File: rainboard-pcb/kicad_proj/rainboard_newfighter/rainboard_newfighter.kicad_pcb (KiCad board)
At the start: 2 copper layers, 260 x 253.6 mm, 97 parts, among them J1 Conn_01x02, J10 Conn_01x03, J11 SDS-50J, J12 SDS-50J, J13 Conn_01x02, J14 Conn_01x02, J15 Conn_01x02, J16 Conn_01x02, J2 Conn_01x02, J3 Conn_01x02, J4 Conn_01x02, J5 Conn_01x02, J6 Conn_01x02, J7 Conn_01x02, J8 Conn_01x02, U1 MCP23017-E_SO, U2 74HC14D, U3 6N138SDM

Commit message: Schematic nearly finalized; PCB / footprint started
-Schematic is nearly finished. Needs some footprint associations and verifications.
-A few open questions remain.
-some lib updates to go w/ sch improvements
-
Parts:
- added C1: 10uF 25V, Capacitor_SMD:C_1206_3216Metric, F.Cu at (150.9, -87.0)
- added C10: 1uF 25V, Capacitor_SMD:C_0805_2012Metric, F.Cu at (167.7, -96.4)
- added C100: 10uF 25V, Capacitor_SMD:C_1206_3216Metric, F.Cu at (135.9, -76.4)
- added C101: 10uF 25V, Capacitor_SMD:C_1206_3216Metric, F.Cu at (135.9, -79.7)
- added C102: 100nf, Capacitor_SMD:C_0603_1608Metric, F.Cu at (290.8, -123.2)
- added C103: 100nf, Capacitor_SMD:C_0603_1608Metric, F.Cu at (204.9, -40.8)
- added C104: 100nf, Capacitor_SMD:C_0603_1608Metric, F.Cu at (264.7, -99.9)
- added C105: 100nf, Capacitor_SMD:C_0603_1608Metric, F.Cu at (232.7, -69.2)
- added C106: 100nf, Capacitor_SMD:C_0603_1608Metric, F.Cu at (250.9, -83.4)
- added C107: 100nf, Capacitor_SMD:C_0603_1608Metric, F.Cu at (220.9, -51.6)
- added C108: 100nf, Capacitor_SMD:C_0603_1608Metric, F.Cu at (280.7, -110.7)
- added C109: 100nf, Capacitor_SMD:C_0603_1608Metric, F.Cu at (201.1, -30.5)
- added C11: 1uF 25V, Capacitor_SMD:C_0805_2012Metric, F.Cu at (172.4, 57.7)
- added C110: 100nf, Capacitor_SMD:C_0603_1608Metric, F.Cu at (250.9, -73.1)
- added C111: 100nf, Capacitor_SMD:C_0603_1608Metric, F.Cu at (306.9, -123.2)
- added C112: 100nf, Capacitor_SMD:C_0603_1608Metric, F.Cu at (185.1, -36.5)
- added C113: 100nf, Capacitor_SMD:C_0603_1608Metric, F.Cu at (280.7, -100.4)
- added C114: 100nf, Capacitor_SMD:C_0603_1608Metric, F.Cu at (217.1, -20.2)
- added C115: 100nf, Capacitor_SMD:C_0603_1608Metric, F.Cu at (266.9, -69.0)
- added C116: 100nf, Capacitor_SMD:C_0603_1608Metric, F.Cu at (237.0, -38.2)
- added C117: 100nf, Capacitor_SMD:C_0603_1608Metric, F.Cu at (322.9, -123.2)
- added C118: 100nf, Capacitor_SMD:C_0603_1608Metric, F.Cu at (283.0, -90.1)
- added C119: 100nf, Capacitor_SMD:C_0603_1608Metric, F.Cu at (237.0, -48.5)
- added C12: 100nf, Capacitor_SMD:C_0603_1608Metric, F.Cu at (186.7, -101.8)
- added C120: 100nf, Capacitor_SMD:C_0603_1608Metric, F.Cu at (266.9, -79.3)
- added C121: 100nf, Capacitor_SMD:C_0603_1608Metric, F.Cu at (217.1, -30.5)
- added C122: 100nf, Capacitor_SMD:C_0603_1608Metric, F.Cu at (296.8, -112.9)
- added C123: 100nf, Capacitor_SMD:C_0603_1608Metric, F.Cu at (237.0, -58.8)
- added C124: 100nf, Capacitor_SMD:C_0603_1608Metric, F.Cu at (266.9, -89.6)
- added C125: 100nf, Capacitor_SMD:C_0603_1608Metric, F.Cu at (220.9, -41.3)
- added C126: 100nf, Capacitor_SMD:C_0603_1608Metric, F.Cu at (269.0, -48.3)
- added C127: 100nf, Capacitor_SMD:C_0603_1608Metric, F.Cu at (312.8, -112.9)
- added C128: 100nf, Capacitor_SMD:C_0603_1608Metric, F.Cu at (283.0, -79.8)
- added C129: 100nf, Capacitor_SMD:C_0603_1608Metric, F.Cu at (253.0, -58.6)
- added C13: 1uF 25V, Capacitor_SMD:C_0805_2012Metric, F.Cu at (176.8, 57.7)
- added C130: 100nf, Capacitor_SMD:C_0603_1608Metric, F.Cu at (299.0, -92.3)
- added C131: 100nf, Capacitor_SMD:C_0603_1608Metric, F.Cu at (253.0, -48.3)
- added C132: 100nf, Capacitor_SMD:C_0603_1608Metric, F.Cu at (233.1, -27.9)
- added C133: 100nf, Capacitor_SMD:C_0603_1608Metric, F.Cu at (253.0, -38.0)
- added C134: 100nf, Capacitor_SMD:C_0603_1608Metric, F.Cu at (269.0, -58.6)
- added C135: 100nf, Capacitor_SMD:C_0603_1608Metric, F.Cu at (283.0, -69.5)
- added C136: 100nf, Capacitor_SMD:C_0603_1608Metric, F.Cu at (312.8, -102.6)
- added C137: 100nf, Capacitor_SMD:C_0603_1608Metric, F.Cu at (328.8, -112.9)
- added C138: 100nf, Capacitor_SMD:C_0603_1608Metric, F.Cu at (299.0, -82.0)
- added C139: 100nf, Capacitor_SMD:C_0603_1608Metric, F.Cu at (315.0, -92.3)
- added C14: 470uF 25V, Capacitor_SMD:CP_Elec_10x10, F.Cu at (236.1, -5.10)
- added C140: 100nf, Capacitor_SMD:C_0603_1608Metric, F.Cu at (296.8, -102.6)
- added C141: 100nf, Capacitor_SMD:C_0603_1608Metric, F.Cu at (249.1, -27.7)
- added C142: 100nf, Capacitor_SMD:C_0603_1608Metric, F.Cu at (269.0, -38.0)
- added C143: 100nf, Capacitor_SMD:C_0603_1608Metric, F.Cu at (299.0, -71.6)
- added C144: 100nf, Capacitor_SMD:C_0603_1608Metric, F.Cu at (328.8, -102.6)
- added C145: 100nf, Capacitor_SMD:C_0603_1608Metric, F.Cu at (285.0, -59.1)
- added C146: 100nf, Capacitor_SMD:C_0603_1608Metric, F.Cu at (315.0, -82.0)
- added C147: 100nf, Capacitor_SMD:C_0603_1608Metric, F.Cu at (331.0, -92.3)
- added C148: 100nf, Capacitor_SMD:C_0603_1608Metric, F.Cu at (285.0, -48.8)
- added C149: 100nf, Capacitor_SMD:C_0603_1608Metric, F.Cu at (265.2, -27.7)
- added C15: 1uF 25V, Capacitor_SMD:C_0805_2012Metric, F.Cu at (188.0, -118.1)
- added C150: 100nf, Capacitor_SMD:C_0603_1608Metric, F.Cu at (285.0, -38.5)
- added C151: 100nf, Capacitor_SMD:C_0603_1608Metric, F.Cu at (315.0, -71.6)
- added C152: 100nf, Capacitor_SMD:C_0603_1608Metric, F.Cu at (301.0, -61.3)
- added C153: 100nf, Capacitor_SMD:C_0603_1608Metric, F.Cu at (331.0, -82.0)
- added C154: 100nf, Capacitor_SMD:C_0603_1608Metric, F.Cu at (201.1, -20.2)
- added C155: 100nf, Capacitor_SMD:C_0603_1608Metric, F.Cu at (244.0, -93.7)
- added C156: 100nf, Capacitor_SMD:C_0603_1608Metric, F.Cu at (264.7, -110.2)
- added C157: 100nf, Capacitor_SMD:C_0603_1608Metric, F.Cu at (204.9, -51.1)
- added C158: 100nf, Capacitor_SMD:C_0603_1608Metric, F.Cu at (185.1, -26.2)
- added C16: 22PF, Capacitor_SMD:C_0603_1608Metric, F.Cu at (184.2, -99.1)
- added C17: 22PF, Capacitor_SMD:C_0603_1608Metric, F.Cu at (193.1, -107.9)
- added C18: 1uF 25V, Capacitor_SMD:C_0805_2012Metric, F.Cu at (179.5, -110.8)
- added C19: 100nf, Capacitor_SMD:C_0603_1608Metric, F.Cu at (188.7, -104.3)
- added C20: 470uF 25V, Capacitor_SMD:CP_Elec_10x10, F.Cu at (236.1, 6.75)
- added C21: 1uF 25V, Capacitor_SMD:C_0805_2012Metric, F.Cu at (155.9, -85.9)
- added C22: 10uF 25V, Capacitor_SMD:C_1206_3216Metric, F.Cu at (180.1, -114.0)
- added C23: 1uF 25V, Capacitor_SMD:C_0805_2012Metric, F.Cu at (181.2, 57.7)
- added C24: 10uF 25V, Capacitor_SMD:C_1206_3216Metric, F.Cu at (156.9, -92.9)
- added C25: 10uF 25V, Capacitor_SMD:C_1206_3216Metric, F.Cu at (150.9, -90.3)
- added C26: 10uF 25V, Capacitor_SMD:C_1206_3216Metric, F.Cu at (160.0, -111.3)
- added C27: 10uF 25V, Capacitor_SMD:C_1206_3216Metric, F.Cu at (162.7, -96.3)
- added C28: 1uF 25V, Capacitor_SMD:C_0805_2012Metric, F.Cu at (194.5, -121.4)
- added C29: 100nf, Capacitor_SMD:C_0603_1608Metric, F.Cu at (182.7, -101.6)
- added C3: 10uF 25V, Capacitor_SMD:C_1206_3216Metric, F.Cu at (182.9, -117.6)
- added C30: 10uF 25V, Capacitor_SMD:C_1206_3216Metric, F.Cu at (190.7, -125.8)
- added C31: 100nf, Capacitor_SMD:C_0603_1608Metric, F.Cu at (197.7, -116.2)
- added C32: 470uF 25V, Capacitor_SMD:CP_Elec_10x10, F.Cu at (250.2, -5.10)
- added C33: 100nf, Capacitor_SMD:C_0603_1608Metric, F.Cu at (188.7, -106.8)
- added C34: 22PF, Capacitor_SMD:C_0603_1608Metric, F.Cu at (180.2, -99.1)
- added C35: 22PF, Capacitor_SMD:C_0603_1608Metric, F.Cu at (189.1, -109.3)
- added C36: 1uF 25V, Capacitor_SMD:C_0805_2012Metric, F.Cu at (192.4, -118.1)
- added C37: 100nf, Capacitor_SMD:C_0603_1608Metric, F.Cu at (203.9, -123.2)
- added C38: 470uF 25V, Capacitor_SMD:CP_Elec_10x10, F.Cu at (250.2, 6.75)
- added C39: 100nf, Capacitor_SMD:C_0603_1608Metric, F.Cu at (160.1, -85.9)
- added C40: 100nf, Capacitor_SMD:C_0603_1608Metric, F.Cu at (176.2, -97.2)
- added C41: 100nf, Capacitor_SMD:C_0603_1608Metric, F.Cu at (193.7, -115.4)
- added C42: 1uF 25V, Capacitor_SMD:C_0805_2012Metric, F.Cu at (180.5, -107.9)
- added C43: 100nf, Capacitor_SMD:C_0603_1608Metric, F.Cu at (170.7, -93.0)
- added C44: 100nf, Capacitor_SMD:C_0603_1608Metric, F.Cu at (178.7, -101.6)
- added C45: 10uF 25V, Capacitor_SMD:C_1206_3216Metric, F.Cu at (226.8, -119.2)
- added C46: 10uF 25V, Capacitor_SMD:C_1206_3216Metric, F.Cu at (215.6, -125.8)
- added C47: 10uF 25V, Capacitor_SMD:C_1206_3216Metric, F.Cu at (221.2, -115.9)
- added C48: 10uF 25V, Capacitor_SMD:C_1206_3216Metric, F.Cu at (232.4, -125.8)
- added C49: 10uF 25V, Capacitor_SMD:C_1206_3216Metric, F.Cu at (226.8, -122.5)
- added C5: 1uF 25V, Capacitor_SMD:C_0805_2012Metric, F.Cu at (189.2, 54.5)
- added C50: 10uF 25V, Capacitor_SMD:C_1206_3216Metric, F.Cu at (221.2, -119.2)
- added C51: 10uF 25V, Capacitor_SMD:C_1206_3216Metric, F.Cu at (215.6, -115.9)
- added C52: 10uF 25V, Capacitor_SMD:C_1206_3216Metric, F.Cu at (226.8, -125.8)
- added C53: 10uF 25V, Capacitor_SMD:C_1206_3216Metric, F.Cu at (221.2, -122.5)
- added C54: 10uF 25V, Capacitor_SMD:C_1206_3216Metric, F.Cu at (215.6, -119.2)
- added C55: 10uF 25V, Capacitor_SMD:C_1206_3216Metric, F.Cu at (221.2, -125.8)
- added C56: 10uF 25V, Capacitor_SMD:C_1206_3216Metric, F.Cu at (215.6, -122.5)
- added C57: DNP-10uF 25V, Capacitor_SMD:C_1206_3216Metric, F.Cu at (215.6, -89.7)
- added C58: 1uF 25V, Capacitor_SMD:C_0805_2012Metric, F.Cu at (220.6, -89.8)
- added C59: DNP-10uF 25V, Capacitor_SMD:C_1206_3216Metric, F.Cu at (236.3, -102.7)
- added C6: 10uF 25V, Capacitor_SMD:C_1206_3216Metric, F.Cu at (182.9, -120.8)
- added C60: 1uF 25V, Capacitor_SMD:C_0805_2012Metric, F.Cu at (244.2, -109.5)
- added C61: DNP-10uF 25V, Capacitor_SMD:C_1206_3216Metric, F.Cu at (135.9, -44.9)
- added C62: 1uF 25V, Capacitor_SMD:C_0805_2012Metric, F.Cu at (140.9, -45.1)
- added C63: DNP-10uF 25V, Capacitor_SMD:C_1206_3216Metric, F.Cu at (183.5, -73.1)
- added C64: 1uF 25V, Capacitor_SMD:C_0805_2012Metric, F.Cu at (188.5, -73.2)
- added C65: DNP-10uF 25V, Capacitor_SMD:C_1206_3216Metric, F.Cu at (135.9, -31.9)
- added C66: 1uF 25V, Capacitor_SMD:C_0805_2012Metric, F.Cu at (143.7, -38.7)
- added C67: DNP-10uF 25V, Capacitor_SMD:C_1206_3216Metric, F.Cu at (215.6, -102.7)
- added C68: 1uF 25V, Capacitor_SMD:C_0805_2012Metric, F.Cu at (223.4, -109.5)
- added C69: DNP-10uF 25V, Capacitor_SMD:C_1206_3216Metric, F.Cu at (156.7, -44.9)
- added C7: 100nf, Capacitor_SMD:C_0603_1608Metric, F.Cu at (180.2, -94.1)
- added C70: 1uF 25V, Capacitor_SMD:C_0805_2012Metric, F.Cu at (164.5, -51.7)
- added C71: DNP-10uF 25V, Capacitor_SMD:C_1206_3216Metric, F.Cu at (242.6, -119.2)
- added C72: 1uF 25V, Capacitor_SMD:C_0805_2012Metric, F.Cu at (250.4, -126.0)
- added C73: DNP-10uF 25V, Capacitor_SMD:C_1206_3216Metric, F.Cu at (135.9, -18.9)
- added C74: 1uF 25V, Capacitor_SMD:C_0805_2012Metric, F.Cu at (143.7, -25.7)
- added C75: DNP-10uF 25V, Capacitor_SMD:C_1206_3216Metric, F.Cu at (183.5, -60.1)
- added C76: 1uF 25V, Capacitor_SMD:C_0805_2012Metric, F.Cu at (191.4, -66.8)
- added C77: DNP-10uF 25V, Capacitor_SMD:C_1206_3216Metric, F.Cu at (204.3, -73.1)
- added C78: 1uF 25V, Capacitor_SMD:C_0805_2012Metric, F.Cu at (212.1, -79.8)
- added C79: DNP-10uF 25V, Capacitor_SMD:C_1206_3216Metric, F.Cu at (156.7, -31.9)
- added C8: 1uF 25V, Capacitor_SMD:C_0805_2012Metric, F.Cu at (166.5, -93.2)
- added C80: 1uF 25V, Capacitor_SMD:C_0805_2012Metric, F.Cu at (161.7, -32.1)
- added C81: 470uF 25V, Capacitor_SMD:CP_Elec_10x10, F.Cu at (236.1, 23.7)
- added C82: 10uF 25V, Capacitor_SMD:C_1206_3216Metric, F.Cu at (225.1, -80.0)
- added C83: 10uF 25V, Capacitor_SMD:C_1206_3216Metric, F.Cu at (225.1, -83.3)
- added C84: 100nf, Capacitor_SMD:C_0603_1608Metric, F.Cu at (203.5, -60.4)
- added C85: 100nf, Capacitor_SMD:C_0603_1608Metric, F.Cu at (155.9, -19.3)
- added C86: 100nf, Capacitor_SMD:C_0603_1608Metric, F.Cu at (275.4, -126.2)
- added C87: 100nf, Capacitor_SMD:C_0603_1608Metric, F.Cu at (189.5, -52.0)
- added C88: 470uF 25V, Capacitor_SMD:CP_Elec_10x10, F.Cu at (285.0, -5.10)
- added C89: 470uF 25V, Capacitor_SMD:CP_Elec_10x10, F.Cu at (285.0, 6.75)
- added C9: 100nf, Capacitor_SMD:C_0603_1608Metric, F.Cu at (201.7, -115.7)
- added C90: 470uF 25V, Capacitor_SMD:CP_Elec_10x10, F.Cu at (299.0, -5.10)
- added C91: 470uF 25V, Capacitor_SMD:CP_Elec_10x10, F.Cu at (299.0, 6.75)
- added C92: 10uF 25V, Capacitor_SMD:C_1206_3216Metric, F.Cu at (135.9, -66.5)
- added C93: 10uF 25V, Capacitor_SMD:C_1206_3216Metric, F.Cu at (147.1, -76.4)
- added C94: 10uF 25V, Capacitor_SMD:C_1206_3216Metric, F.Cu at (141.5, -73.1)
- added C95: 10uF 25V, Capacitor_SMD:C_1206_3216Metric, F.Cu at (135.9, -69.8)
- added C96: 10uF 25V, Capacitor_SMD:C_1206_3216Metric, F.Cu at (147.1, -79.7)
- added C97: 10uF 25V, Capacitor_SMD:C_1206_3216Metric, F.Cu at (141.5, -76.4)
- added C98: 10uF 25V, Capacitor_SMD:C_1206_3216Metric, F.Cu at (135.9, -73.1)
- added C99: 10uF 25V, Capacitor_SMD:C_1206_3216Metric, F.Cu at (141.5, -79.7)
- added D1: 12Vw, Diode_SMD:D_SMA, F.Cu at (137.1, -87.5)
- added D10: 40V 1A, Diode_SMD:D_SOD-123, F.Cu at (157.0, -96.3)
- added D11: 40V 1A, Diode_SMD:D_SOD-123, F.Cu at (153.0, -99.6)
- added D12: 40V 1A, Diode_SMD:D_SOD-123, F.Cu at (174.3, -110.6)
- added D13: 5Vw, Package_TO_SOT_SMD:SOT-23, F.Cu at (176.1, -106.6)
- added D14: 40V 1A, Diode_SMD:D_SOD-123, F.Cu at (154.3, -111.3)
- added D15: 5Vw, Package_TO_SOT_SMD:SOT-23, F.Cu at (162.1, -92.4)
- added D16: 5Vw, Package_TO_SOT_SMD:SOT-23, F.Cu at (190.1, -121.9)
- added D17: 40V 1A, Diode_SMD:D_SOD-123, F.Cu at (158.8, -99.6)
- added D18: 40V 1A, Diode_SMD:D_SOD-123, F.Cu at (165.0, -100.7)
- added D19: WS2812B, LED_SMD:LED_WS2812B_PLCC4_5.0x5.0mm_P3.2mm, F.Cu at (217.0, -94.6)
- added D2: 5Vw, Package_TO_SOT_SMD:SOT-23, F.Cu at (185.1, -113.6)
- added D20: WS2812B, LED_SMD:LED_WS2812B_PLCC4_5.0x5.0mm_P3.2mm, F.Cu at (237.7, -107.6)
- added D21: WS2812B, LED_SMD:LED_WS2812B_PLCC4_5.0x5.0mm_P3.2mm, F.Cu at (0.47, -93.5)
- added D22: WS2812B, LED_SMD:LED_WS2812B_PLCC4_5.0x5.0mm_P3.2mm, F.Cu at (184.9, -78.0)
- added D23: WS2812B, LED_SMD:LED_WS2812B_PLCC4_5.0x5.0mm_P3.2mm, F.Cu at (137.3, -36.9)
- added D24: WS2812B, LED_SMD:LED_WS2812B_PLCC4_5.0x5.0mm_P3.2mm, F.Cu at (217.0, -107.6)
- added D25: WS2812B, LED_SMD:LED_WS2812B_PLCC4_5.0x5.0mm_P3.2mm, F.Cu at (158.1, -49.9)
- added D26: WS2812B, LED_SMD:LED_WS2812B_PLCC4_5.0x5.0mm_P3.2mm, F.Cu at (244.0, -124.1)
- added D27: WS2812B, LED_SMD:LED_WS2812B_PLCC4_5.0x5.0mm_P3.2mm, F.Cu at (137.3, -23.9)
- added D28: WS2812B, LED_SMD:LED_WS2812B_PLCC4_5.0x5.0mm_P3.2mm, F.Cu at (184.9, -65.0)
- added D29: WS2812B, LED_SMD:LED_WS2812B_PLCC4_5.0x5.0mm_P3.2mm, F.Cu at (205.7, -78.0)
- added D3: 5Vw, Package_TO_SOT_SMD:SOT-23, F.Cu at (195.7, -125.2)
- added D30: WS2812B, LED_SMD:LED_WS2812B_PLCC4_5.0x5.0mm_P3.2mm, F.Cu at (158.1, -36.9)
- added D31: WS2812B, LED_SMD:LED_WS2812B_PLCC4_5.0x5.0mm_P3.2mm, F.Cu at (205.7, -65.0)
- added D32: WS2812B, LED_SMD:LED_WS2812B_PLCC4_5.0x5.0mm_P3.2mm, F.Cu at (158.1, -23.9)
- added D33: WS2812B, LED_SMD:LED_WS2812B_PLCC4_5.0x5.0mm_P3.2mm, F.Cu at (264.8, -124.1)
- added D34: WS2812B, LED_SMD:LED_WS2812B_PLCC4_5.0x5.0mm_P3.2mm, F.Cu at (178.9, -49.9)
- added D35: WS2812B, LED_SMD:LED_WS2812B_PLCC4_5.0x5.0mm_P3.2mm, F.Cu at (284.6, -124.1)
- added D36: WS2812B, LED_SMD:LED_WS2812B_PLCC4_5.0x5.0mm_P3.2mm, F.Cu at (198.7, -41.7)
- added D37: WS2812B, LED_SMD:LED_WS2812B_PLCC4_5.0x5.0mm_P3.2mm, F.Cu at (258.5, -100.8)
- added D38: WS2812B, LED_SMD:LED_WS2812B_PLCC4_5.0x5.0mm_P3.2mm, F.Cu at (226.5, -70.1)
- added D39: WS2812B, LED_SMD:LED_WS2812B_PLCC4_5.0x5.0mm_P3.2mm, F.Cu at (244.7, -84.3)
- added D4: 5Vw, Diode_SMD:D_SMA, F.Cu at (150.1, -94.2)
- added D40: WS2812B, LED_SMD:LED_WS2812B_PLCC4_5.0x5.0mm_P3.2mm, F.Cu at (214.7, -52.5)
- added D41: WS2812B, LED_SMD:LED_WS2812B_PLCC4_5.0x5.0mm_P3.2mm, F.Cu at (274.5, -111.6)
- added D42: WS2812B, LED_SMD:LED_WS2812B_PLCC4_5.0x5.0mm_P3.2mm, F.Cu at (194.9, -31.4)
- added D43: WS2812B, LED_SMD:LED_WS2812B_PLCC4_5.0x5.0mm_P3.2mm, F.Cu at (244.7, -74.0)
- added D44: WS2812B, LED_SMD:LED_WS2812B_PLCC4_5.0x5.0mm_P3.2mm, F.Cu at (300.6, -124.1)
- added D45: WS2812B, LED_SMD:LED_WS2812B_PLCC4_5.0x5.0mm_P3.2mm, F.Cu at (178.9, -37.4)
- added D46: WS2812B, LED_SMD:LED_WS2812B_PLCC4_5.0x5.0mm_P3.2mm, F.Cu at (274.5, -101.3)
- added D47: WS2812B, LED_SMD:LED_WS2812B_PLCC4_5.0x5.0mm_P3.2mm, F.Cu at (210.9, -21.1)
- added D48: WS2812B, LED_SMD:LED_WS2812B_PLCC4_5.0x5.0mm_P3.2mm, F.Cu at (260.7, -69.9)
- added D49: WS2812B, LED_SMD:LED_WS2812B_PLCC4_5.0x5.0mm_P3.2mm, F.Cu at (230.8, -39.1)
- added D5: 12Vw, Diode_SMD:D_SMA, F.Cu at (167.4, -112.0)
- added D50: WS2812B, LED_SMD:LED_WS2812B_PLCC4_5.0x5.0mm_P3.2mm, F.Cu at (316.7, -124.1)
- added D51: WS2812B, LED_SMD:LED_WS2812B_PLCC4_5.0x5.0mm_P3.2mm, F.Cu at (276.7, -91.0)
- added D52: WS2812B, LED_SMD:LED_WS2812B_PLCC4_5.0x5.0mm_P3.2mm, F.Cu at (230.8, -49.4)
- added D53: WS2812B, LED_SMD:LED_WS2812B_PLCC4_5.0x5.0mm_P3.2mm, F.Cu at (260.7, -80.2)
- added D54: WS2812B, LED_SMD:LED_WS2812B_PLCC4_5.0x5.0mm_P3.2mm, F.Cu at (210.9, -31.4)
- added D55: WS2812B, LED_SMD:LED_WS2812B_PLCC4_5.0x5.0mm_P3.2mm, F.Cu at (290.6, -113.8)
- added D56: WS2812B, LED_SMD:LED_WS2812B_PLCC4_5.0x5.0mm_P3.2mm, F.Cu at (230.8, -59.7)
- added D57: WS2812B, LED_SMD:LED_WS2812B_PLCC4_5.0x5.0mm_P3.2mm, F.Cu at (260.7, -90.5)
- added D58: WS2812B, LED_SMD:LED_WS2812B_PLCC4_5.0x5.0mm_P3.2mm, F.Cu at (214.7, -42.2)
- added D59: WS2812B, LED_SMD:LED_WS2812B_PLCC4_5.0x5.0mm_P3.2mm, F.Cu at (262.8, -49.2)
- added D6: 40V 1A, Diode_SMD:D_SOD-123, F.Cu at (174.4, -113.9)
- added D60: WS2812B, LED_SMD:LED_WS2812B_PLCC4_5.0x5.0mm_P3.2mm, F.Cu at (306.6, -113.8)
- added D61: WS2812B, LED_SMD:LED_WS2812B_PLCC4_5.0x5.0mm_P3.2mm, F.Cu at (276.7, -80.7)
- added D62: WS2812B, LED_SMD:LED_WS2812B_PLCC4_5.0x5.0mm_P3.2mm, F.Cu at (246.8, -59.5)
- added D63: WS2812B, LED_SMD:LED_WS2812B_PLCC4_5.0x5.0mm_P3.2mm, F.Cu at (292.8, -93.2)
- added D64: WS2812B, LED_SMD:LED_WS2812B_PLCC4_5.0x5.0mm_P3.2mm, F.Cu at (246.8, -49.2)
- added D65: WS2812B, LED_SMD:LED_WS2812B_PLCC4_5.0x5.0mm_P3.2mm, F.Cu at (226.9, -28.8)
- added D66: WS2812B, LED_SMD:LED_WS2812B_PLCC4_5.0x5.0mm_P3.2mm, F.Cu at (246.8, -38.9)
- added D67: WS2812B, LED_SMD:LED_WS2812B_PLCC4_5.0x5.0mm_P3.2mm, F.Cu at (262.8, -59.5)
- added D68: WS2812B, LED_SMD:LED_WS2812B_PLCC4_5.0x5.0mm_P3.2mm, F.Cu at (276.7, -70.4)
- added D69: WS2812B, LED_SMD:LED_WS2812B_PLCC4_5.0x5.0mm_P3.2mm, F.Cu at (306.6, -103.5)
- added D7: 5Vw, Package_TO_SOT_SMD:SOT-23, F.Cu at (171.6, -106.6)
- added D70: WS2812B, LED_SMD:LED_WS2812B_PLCC4_5.0x5.0mm_P3.2mm, F.Cu at (322.6, -113.8)
- added D71: WS2812B, LED_SMD:LED_WS2812B_PLCC4_5.0x5.0mm_P3.2mm, F.Cu at (292.8, -82.9)
- added D72: WS2812B, LED_SMD:LED_WS2812B_PLCC4_5.0x5.0mm_P3.2mm, F.Cu at (308.8, -93.2)
- added D73: WS2812B, LED_SMD:LED_WS2812B_PLCC4_5.0x5.0mm_P3.2mm, F.Cu at (290.6, -103.5)
- added D74: WS2812B, LED_SMD:LED_WS2812B_PLCC4_5.0x5.0mm_P3.2mm, F.Cu at (242.9, -28.6)
- added D75: WS2812B, LED_SMD:LED_WS2812B_PLCC4_5.0x5.0mm_P3.2mm, F.Cu at (262.8, -38.9)
- added D76: WS2812B, LED_SMD:LED_WS2812B_PLCC4_5.0x5.0mm_P3.2mm, F.Cu at (292.8, -72.5)
- added D77: WS2812B, LED_SMD:LED_WS2812B_PLCC4_5.0x5.0mm_P3.2mm, F.Cu at (322.6, -103.5)
- added D78: WS2812B, LED_SMD:LED_WS2812B_PLCC4_5.0x5.0mm_P3.2mm, F.Cu at (278.8, -60.0)
- added D79: WS2812B, LED_SMD:LED_WS2812B_PLCC4_5.0x5.0mm_P3.2mm, F.Cu at (308.8, -82.9)
- added D8: 5Vw, Package_TO_SOT_SMD:SOT-23, F.Cu at (170.1, -100.1)
- added D80: WS2812B, LED_SMD:LED_WS2812B_PLCC4_5.0x5.0mm_P3.2mm, F.Cu at (324.8, -93.2)
- added D81: WS2812B, LED_SMD:LED_WS2812B_PLCC4_5.0x5.0mm_P3.2mm, F.Cu at (278.8, -49.7)
- added D82: WS2812B, LED_SMD:LED_WS2812B_PLCC4_5.0x5.0mm_P3.2mm, F.Cu at (259.0, -28.6)
- added D83: WS2812B, LED_SMD:LED_WS2812B_PLCC4_5.0x5.0mm_P3.2mm, F.Cu at (278.8, -39.4)
- added D84: WS2812B, LED_SMD:LED_WS2812B_PLCC4_5.0x5.0mm_P3.2mm, F.Cu at (308.8, -72.5)
- added D85: WS2812B, LED_SMD:LED_WS2812B_PLCC4_5.0x5.0mm_P3.2mm, F.Cu at (294.8, -62.2)
- added D86: WS2812B, LED_SMD:LED_WS2812B_PLCC4_5.0x5.0mm_P3.2mm, F.Cu at (324.8, -82.9)
- added D87: WS2812B, LED_SMD:LED_WS2812B_PLCC4_5.0x5.0mm_P3.2mm, F.Cu at (194.9, -21.1)
- added D88: WS2812B, LED_SMD:LED_WS2812B_PLCC4_5.0x5.0mm_P3.2mm, F.Cu at (237.7, -94.6)
- added D89: WS2812B, LED_SMD:LED_WS2812B_PLCC4_5.0x5.0mm_P3.2mm, F.Cu at (258.5, -111.1)
- added D9: 5Vw, Diode_SMD:D_SMA, F.Cu at (176.9, -125.2)
- added D90: WS2812B, LED_SMD:LED_WS2812B_PLCC4_5.0x5.0mm_P3.2mm, F.Cu at (198.7, -52.0)
- added D91: WS2812B, LED_SMD:LED_WS2812B_PLCC4_5.0x5.0mm_P3.2mm, F.Cu at (178.9, -27.1)
- added F1: 20V 3A, Fuse:Fuse_1812_4532Metric, F.Cu at (144.6, -87.3)
- added F2: 15V .5A, Fuse:Fuse_1812_4532Metric, F.Cu at (184.4, -125.0)
- added FB1: 4A Ferrite, Inductor_SMD:L_1206_3216Metric, F.Cu at (173.0, 54.6)
- added FB2: 4A Ferrite, Inductor_SMD:L_1206_3216Metric, F.Cu at (178.6, 54.6)
- added FB3: 4A Ferrite, Inductor_SMD:L_1206_3216Metric, F.Cu at (184.2, 54.6)
- added J1: EJ508A, Connector_BarrelJack:BarrelJack_Horizontal, F.Cu at (147.6, -103.7)
- added J3: Conn_01x03, Connector_JST:JST_XH_B3B-XH-AM_1x03_P2.50mm_Vertical, F.Cu at (153.6, -105.7)
- added J4: Conn_01x03, Connector_JST:JST_XH_B3B-XH-AM_1x03_P2.50mm_Vertical, F.Cu at (154.9, -117.4)
- added J6: SDS-50J, SDS-50J:CUI_SDS-50J, F.Cu at (172.2, 39.7)
- added J7: SDS-50J, SDS-50J:CUI_SDS-50J, F.Cu at (194.5, 39.7)
- added JP1: Jumper, Jumper:SolderJumper-2_P1.3mm_Bridged_Pad1.0x1.5mm, F.Cu at (180.5, -104.6)
- added JP2: Jumper, Jumper:SolderJumper-2_P1.3mm_Bridged_Pad1.0x1.5mm, F.Cu at (189.5, -114.9)
- added JP3: Jumper, Jumper:SolderJumper-2_P1.3mm_Bridged_Pad1.0x1.5mm, F.Cu at (172.0, -96.1)
- added JP4: Jumper, Jumper:SolderJumper-2_P1.3mm_Bridged_Pad1.0x1.5mm, F.Cu at (171.0, 5.96)
- added JP5: Jumper, Jumper:SolderJumper-2_P1.3mm_Bridged_Pad1.0x1.5mm, F.Cu at (175.4, 5.96)
- added L1: 27uH, Inductor_SMD:L_Bourns_SRR1210A, F.Cu at (176.1, -2.59)
- added L3: 27uH, Inductor_SMD:L_Bourns_SRR1210A, F.Cu at (190.5, -2.59)
- added Q1: DUAL 30V NMOS, Package_TO_SOT_SMD:SOT-363_SC-70-6, F.Cu at (185.5, 58.2)
- added Q2: DUAL 30V NMOS, Package_TO_SOT_SMD:SOT-363_SC-70-6, F.Cu at (193.5, 54.9)
- added Q3: 30V 10mOhm, Package_SO:PowerPAK_SO-8_Single, F.Cu at (167.5, -117.5)
- added R10: 100k, Resistor_SMD:R_0603_1608Metric, F.Cu at (201.7, -118.2)
- added R100: 210R, Resistor_SMD:R_0805_2012Metric, F.Cu at (174.2, -79.8)
- added R101: 210R, Resistor_SMD:R_0805_2012Metric, F.Cu at (158.6, -65.1)
- added R102: 210R, Resistor_SMD:R_0805_2012Metric, F.Cu at (144.1, -58.2)
- added R103: 210R, Resistor_SMD:R_0805_2012Metric, F.Cu at (149.7, -67.4)
- added R104: 210R, Resistor_SMD:R_0805_2012Metric, F.Cu at (140.9, -67.0)
- added R105: 210R, Resistor_SMD:R_0805_2012Metric, F.Cu at (155.3, -73.9)
- added R106: 210R, Resistor_SMD:R_0805_2012Metric, F.Cu at (135.3, -63.4)
- added R107: 210R, Resistor_SMD:R_0805_2012Metric, F.Cu at (144.1, -61.1)
- added R108: 210R, Resistor_SMD:R_0805_2012Metric, F.Cu at (154.1, -70.3)
- added R109: 210R, Resistor_SMD:R_0805_2012Metric, F.Cu at (165.4, -79.8)
- added R11: 100k, Resistor_SMD:R_0603_1608Metric, F.Cu at (174.3, -90.5)
- added R110: 210R, Resistor_SMD:R_0805_2012Metric, F.Cu at (149.7, -64.4)
- added R111: 210R, Resistor_SMD:R_0805_2012Metric, F.Cu at (159.8, -73.9)
- added R112: 210R, Resistor_SMD:R_0805_2012Metric, F.Cu at (161.0, -79.8)
- added R113: 210R, Resistor_SMD:R_0805_2012Metric, F.Cu at (161.0, -76.9)
- added R114: 210R, Resistor_SMD:R_0805_2012Metric, F.Cu at (167.4, -62.1)
- added R115: 210R, Resistor_SMD:R_0805_2012Metric, F.Cu at (144.1, -64.1)
- added R116: 210R, Resistor_SMD:R_0805_2012Metric, F.Cu at (152.9, -58.5)
- added R117: 210R, Resistor_SMD:R_0805_2012Metric, F.Cu at (156.5, -76.9)
- added R118: 210R, Resistor_SMD:R_0805_2012Metric, F.Cu at (150.9, -73.3)
- added R119: 210R, Resistor_SMD:R_0805_2012Metric, F.Cu at (139.7, -63.4)
- added R12: 100k, Resistor_SMD:R_0603_1608Metric, F.Cu at (178.3, -91.6)
- added R120: 210R, Resistor_SMD:R_0805_2012Metric, F.Cu at (156.5, -79.8)
- added R121: 210R, Resistor_SMD:R_0805_2012Metric, F.Cu at (135.3, -60.4)
- added R122: 210R, Resistor_SMD:R_0805_2012Metric, F.Cu at (171.8, -68.0)
- added R123: 210R, Resistor_SMD:R_0805_2012Metric, F.Cu at (145.3, -70.0)
- added R124: 210R, Resistor_SMD:R_0805_2012Metric, F.Cu at (152.1, -76.9)
- added R125: 210R, Resistor_SMD:R_0805_2012Metric, F.Cu at (146.5, -73.3)
- added R126: 210R, Resistor_SMD:R_0805_2012Metric, F.Cu at (140.9, -70.0)
- added R127: 210R, Resistor_SMD:R_0805_2012Metric, F.Cu at (152.1, -79.8)
- added R128: 210R, Resistor_SMD:R_0805_2012Metric, F.Cu at (139.7, -60.4)
- added R129: 210R, Resistor_SMD:R_0805_2012Metric, F.Cu at (145.3, -67.0)
- added R13: 19.1k, Resistor_SMD:R_0603_1608Metric, F.Cu at (205.7, -118.2)
- added R130: 210R, Resistor_SMD:R_0805_2012Metric, F.Cu at (149.7, -70.3)
- added R131: 210R, Resistor_SMD:R_0805_2012Metric, F.Cu at (291.0, -126.0)
- added R132: 210R, Resistor_SMD:R_0805_2012Metric, F.Cu at (205.1, -43.5)
- added R133: 210R, Resistor_SMD:R_0805_2012Metric, F.Cu at (264.9, -102.6)
- added R134: 210R, Resistor_SMD:R_0805_2012Metric, F.Cu at (232.9, -71.9)
- added R135: 210R, Resistor_SMD:R_0805_2012Metric, F.Cu at (251.1, -86.1)
- added R136: 210R, Resistor_SMD:R_0805_2012Metric, F.Cu at (221.1, -54.4)
- added R137: 210R, Resistor_SMD:R_0805_2012Metric, F.Cu at (280.9, -113.5)
- added R138: 210R, Resistor_SMD:R_0805_2012Metric, F.Cu at (201.3, -33.2)
- added R139: 210R, Resistor_SMD:R_0805_2012Metric, F.Cu at (251.1, -75.8)
- added R14: 100k, Resistor_SMD:R_0603_1608Metric, F.Cu at (180.2, -96.6)
- added R140: 210R, Resistor_SMD:R_0805_2012Metric, F.Cu at (307.1, -126.0)
- added R141: 210R, Resistor_SMD:R_0805_2012Metric, F.Cu at (185.3, -39.2)
- added R142: 210R, Resistor_SMD:R_0805_2012Metric, F.Cu at (280.9, -103.2)
- added R143: 210R, Resistor_SMD:R_0805_2012Metric, F.Cu at (217.3, -22.9)
- added R144: 210R, Resistor_SMD:R_0805_2012Metric, F.Cu at (267.1, -71.7)
- added R145: 210R, Resistor_SMD:R_0805_2012Metric, F.Cu at (237.2, -40.9)
- added R146: 210R, Resistor_SMD:R_0805_2012Metric, F.Cu at (323.1, -126.0)
- added R147: 210R, Resistor_SMD:R_0805_2012Metric, F.Cu at (283.2, -92.8)
- added R148: 210R, Resistor_SMD:R_0805_2012Metric, F.Cu at (237.2, -51.3)
- added R149: 210R, Resistor_SMD:R_0805_2012Metric, F.Cu at (267.1, -82.0)
- added R15: 210R, Resistor_SMD:R_0805_2012Metric, F.Cu at (174.5, -102.9)
- added R150: 210R, Resistor_SMD:R_0805_2012Metric, F.Cu at (217.3, -33.2)
- added R151: 210R, Resistor_SMD:R_0805_2012Metric, F.Cu at (297.0, -115.6)
- added R152: 210R, Resistor_SMD:R_0805_2012Metric, F.Cu at (237.2, -61.6)
- added R153: 210R, Resistor_SMD:R_0805_2012Metric, F.Cu at (267.1, -92.3)
- added R154: 210R, Resistor_SMD:R_0805_2012Metric, F.Cu at (221.1, -44.0)
- added R155: 210R, Resistor_SMD:R_0805_2012Metric, F.Cu at (269.2, -51.0)
- added R156: 210R, Resistor_SMD:R_0805_2012Metric, F.Cu at (313.0, -115.6)
- added R157: 210R, Resistor_SMD:R_0805_2012Metric, F.Cu at (283.2, -82.5)
- added R158: 210R, Resistor_SMD:R_0805_2012Metric, F.Cu at (253.2, -61.4)
- added R159: 210R, Resistor_SMD:R_0805_2012Metric, F.Cu at (299.2, -95.0)
- added R16: 100k, Resistor_SMD:R_0603_1608Metric, F.Cu at (184.6, -104.6)
- added R160: 210R, Resistor_SMD:R_0805_2012Metric, F.Cu at (253.2, -51.0)
- added R161: 210R, Resistor_SMD:R_0805_2012Metric, F.Cu at (233.3, -30.6)
- added R162: 210R, Resistor_SMD:R_0805_2012Metric, F.Cu at (253.2, -40.7)
- added R163: 210R, Resistor_SMD:R_0805_2012Metric, F.Cu at (269.2, -61.4)
- added R164: 210R, Resistor_SMD:R_0805_2012Metric, F.Cu at (283.2, -72.2)
- added R165: 210R, Resistor_SMD:R_0805_2012Metric, F.Cu at (313.0, -105.3)
- added R166: 210R, Resistor_SMD:R_0805_2012Metric, F.Cu at (329.0, -115.6)
- added R167: 210R, Resistor_SMD:R_0805_2012Metric, F.Cu at (299.2, -84.7)
- added R168: 210R, Resistor_SMD:R_0805_2012Metric, F.Cu at (315.2, -95.0)
- added R169: 210R, Resistor_SMD:R_0805_2012Metric, F.Cu at (297.0, -105.3)
- added R17: 11R, Resistor_SMD:R_0603_1608Metric, F.Cu at (169.1, -87.9)
- added R170: 210R, Resistor_SMD:R_0805_2012Metric, F.Cu at (249.3, -30.4)
- added R171: 210R, Resistor_SMD:R_0805_2012Metric, F.Cu at (269.2, -40.7)
- added R172: 210R, Resistor_SMD:R_0805_2012Metric, F.Cu at (299.2, -74.4)
- added R173: 210R, Resistor_SMD:R_0805_2012Metric, F.Cu at (329.0, -105.3)
- added R174: 210R, Resistor_SMD:R_0805_2012Metric, F.Cu at (285.2, -61.9)
- added R175: 210R, Resistor_SMD:R_0805_2012Metric, F.Cu at (315.2, -84.7)
- added R176: 210R, Resistor_SMD:R_0805_2012Metric, F.Cu at (331.2, -95.0)
- added R177: 210R, Resistor_SMD:R_0805_2012Metric, F.Cu at (285.2, -51.6)
- added R178: 210R, Resistor_SMD:R_0805_2012Metric, F.Cu at (265.4, -30.4)
- added R179: 210R, Resistor_SMD:R_0805_2012Metric, F.Cu at (285.2, -41.2)
- added R18: DNP-4.7k, Resistor_SMD:R_0603_1608Metric, F.Cu at (193.7, -112.9)
- added R180: 210R, Resistor_SMD:R_0805_2012Metric, F.Cu at (315.2, -74.4)
- added R181: 210R, Resistor_SMD:R_0805_2012Metric, F.Cu at (301.2, -64.0)
- added R182: 210R, Resistor_SMD:R_0805_2012Metric, F.Cu at (331.2, -84.7)
- added R183: 210R, Resistor_SMD:R_0805_2012Metric, F.Cu at (201.3, -22.9)
- added R184: 210R, Resistor_SMD:R_0805_2012Metric, F.Cu at (244.2, -96.5)
- added R185: 210R, Resistor_SMD:R_0805_2012Metric, F.Cu at (264.9, -113.0)
- added R186: 210R, Resistor_SMD:R_0805_2012Metric, F.Cu at (205.1, -53.8)
- added R187: 210R, Resistor_SMD:R_0805_2012Metric, F.Cu at (185.3, -28.9)
- added R19: 4.7k, Resistor_SMD:R_0603_1608Metric, F.Cu at (176.2, -94.7)
- added R20: 11R, Resistor_SMD:R_0603_1608Metric, F.Cu at (200.6, -120.7)
- added R22: 11R, Resistor_SMD:R_0603_1608Metric, F.Cu at (184.7, -107.2)
- added R23: 210R, Resistor_SMD:R_0805_2012Metric, F.Cu at (200.1, -126.0)
- added R24: 19.1k, Resistor_SMD:R_0603_1608Metric, F.Cu at (201.7, -113.2)
- added R25: 210R, Resistor_SMD:R_0805_2012Metric, F.Cu at (160.8, -88.6)
- added R26: DNP-210R, Resistor_SMD:R_0805_2012Metric, F.Cu at (174.5, -99.9)
- added R27: 19.1k, Resistor_SMD:R_0603_1608Metric, F.Cu at (184.2, -96.6)
- added R28: 19.1k, Resistor_SMD:R_0603_1608Metric, F.Cu at (197.7, -111.2)
- added R29: 11R, Resistor_SMD:R_0603_1608Metric, F.Cu at (197.1, -107.9)
- added R30: 210R, Resistor_SMD:R_0805_2012Metric, F.Cu at (184.9, -109.9)
- added R31: 11R, Resistor_SMD:R_0603_1608Metric, F.Cu at (190.7, -101.8)
- added R32: 4.7k, Resistor_SMD:R_0603_1608Metric, F.Cu at (177.1, -88.0)
- added R33: 4.7k, Resistor_SMD:R_0603_1608Metric, F.Cu at (188.3, -99.3)
- added R34: 19.1k, Resistor_SMD:R_0603_1608Metric, F.Cu at (170.3, -90.4)
- added R35: 4.7k, Resistor_SMD:R_0603_1608Metric, F.Cu at (166.3, -90.4)
- added R36: 11R, Resistor_SMD:R_0603_1608Metric, F.Cu at (199.9, -123.2)
- added R37: 11R, Resistor_SMD:R_0603_1608Metric, F.Cu at (196.6, -118.7)
- added R38: 11R, Resistor_SMD:R_0603_1608Metric, F.Cu at (189.4, -111.8)
- added R39: 11R, Resistor_SMD:R_0603_1608Metric, F.Cu at (192.7, -105.4)
- added R40: 19.1k, Resistor_SMD:R_0603_1608Metric, F.Cu at (204.3, -126.2)
- added R41: 4.7k, Resistor_SMD:R_0603_1608Metric, F.Cu at (165.0, -87.9)
- added R42: 220R, Resistor_SMD:R_0805_2012Metric, F.Cu at (223.4, -96.5)
- added R43: 220R, Resistor_SMD:R_0805_2012Metric, F.Cu at (241.3, -102.8)
- added R44: 220R, Resistor_SMD:R_0805_2012Metric, F.Cu at (143.7, -51.7)
- added R45: 220R, Resistor_SMD:R_0805_2012Metric, F.Cu at (191.4, -79.8)
- added R46: 220R, Resistor_SMD:R_0805_2012Metric, F.Cu at (140.9, -32.1)
- added R47: 220R, Resistor_SMD:R_0805_2012Metric, F.Cu at (220.6, -102.8)
- added R48: 220R, Resistor_SMD:R_0805_2012Metric, F.Cu at (161.7, -45.1)
- added R49: 220R, Resistor_SMD:R_0805_2012Metric, F.Cu at (247.6, -119.3)
- added R50: 220R, Resistor_SMD:R_0805_2012Metric, F.Cu at (140.9, -19.1)
- added R51: 220R, Resistor_SMD:R_0805_2012Metric, F.Cu at (188.5, -60.2)
- added R52: 220R, Resistor_SMD:R_0805_2012Metric, F.Cu at (209.3, -73.2)
- added R53: 220R, Resistor_SMD:R_0805_2012Metric, F.Cu at (164.5, -38.7)
- added R54: 210R, Resistor_SMD:R_0805_2012Metric, F.Cu at (234.5, -80.5)
- added R55: 210R, Resistor_SMD:R_0805_2012Metric, F.Cu at (234.5, -83.5)
- added R56: 210R, Resistor_SMD:R_0805_2012Metric, F.Cu at (230.1, -80.5)
- added R57: 210R, Resistor_SMD:R_0805_2012Metric, F.Cu at (230.1, -83.5)
- added R58: 210R, Resistor_SMD:R_0805_2012Metric, F.Cu at (212.1, -66.8)
- added R59: 4.7k, Resistor_SMD:R_0603_1608Metric, F.Cu at (216.3, -67.1)
- added R6: 11R, Resistor_SMD:R_0603_1608Metric, F.Cu at (193.4, -110.4)
- added R60: 19.1k, Resistor_SMD:R_0603_1608Metric, F.Cu at (207.5, -60.4)
- added R61: 19.1k, Resistor_SMD:R_0603_1608Metric, F.Cu at (211.9, -64.1)
- added R62: 210R, Resistor_SMD:R_0805_2012Metric, F.Cu at (164.5, -25.7)
- added R63: 4.7k, Resistor_SMD:R_0603_1608Metric, F.Cu at (168.7, -26.0)
- added R64: 19.1k, Resistor_SMD:R_0603_1608Metric, F.Cu at (159.9, -19.3)
- added R65: 19.1k, Resistor_SMD:R_0603_1608Metric, F.Cu at (164.3, -23.0)
- added R66: 210R, Resistor_SMD:R_0805_2012Metric, F.Cu at (271.2, -126.0)
- added R67: 4.7k, Resistor_SMD:R_0603_1608Metric, F.Cu at (262.6, -119.6)
- added R68: 19.1k, Resistor_SMD:R_0603_1608Metric, F.Cu at (271.0, -123.2)
- added R69: 19.1k, Resistor_SMD:R_0603_1608Metric, F.Cu at (266.6, -119.6)
- added R7: 11R, Resistor_SMD:R_0603_1608Metric, F.Cu at (204.6, -120.7)
- added R70: 210R, Resistor_SMD:R_0805_2012Metric, F.Cu at (185.3, -51.7)
- added R71: 4.7k, Resistor_SMD:R_0603_1608Metric, F.Cu at (176.6, -45.3)
- added R72: 19.1k, Resistor_SMD:R_0603_1608Metric, F.Cu at (185.1, -49.0)
- added R73: 19.1k, Resistor_SMD:R_0603_1608Metric, F.Cu at (180.7, -45.3)
- added R74: 210R, Resistor_SMD:R_0805_2012Metric, F.Cu at (161.8, -59.2)
- added R75: 210R, Resistor_SMD:R_0805_2012Metric, F.Cu at (167.4, -65.1)
- added R76: 210R, Resistor_SMD:R_0805_2012Metric, F.Cu at (171.8, -71.0)
- added R77: 210R, Resistor_SMD:R_0805_2012Metric, F.Cu at (163.0, -62.1)
- added R78: 210R, Resistor_SMD:R_0805_2012Metric, F.Cu at (167.4, -68.0)
- added R79: 210R, Resistor_SMD:R_0805_2012Metric, F.Cu at (157.4, -59.2)
- added R8: 11R, Resistor_SMD:R_0603_1608Metric, F.Cu at (197.7, -113.7)
- added R80: 210R, Resistor_SMD:R_0805_2012Metric, F.Cu at (173.0, -73.9)
- added R81: 210R, Resistor_SMD:R_0805_2012Metric, F.Cu at (163.0, -65.1)
- added R82: 210R, Resistor_SMD:R_0805_2012Metric, F.Cu at (167.4, -71.0)
- added R83: 210R, Resistor_SMD:R_0805_2012Metric, F.Cu at (158.6, -62.1)
- added R84: 210R, Resistor_SMD:R_0805_2012Metric, F.Cu at (174.2, -76.9)
- added R85: 210R, Resistor_SMD:R_0805_2012Metric, F.Cu at (163.0, -68.0)
- added R86: 210R, Resistor_SMD:R_0805_2012Metric, F.Cu at (154.1, -67.4)
- renumbered R8 to R21
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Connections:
- C1 pad 1: 5V -> 12V_FILT
- C1 pad 2: Earth -> GND
- C3 pad 1: 5V -> 12V_FILT
- C3 pad 2: Earth -> GND
- C4 pad 1: 5V -> 5V_MCU
- C4 pad 2: Earth -> GND
- D1 pad 1: Net-(D1-Pad1) -> Net-(C5-Pad1)
- D1 pad 2: Net-(D1-Pad2) -> GND
- J1 pad 1: Earth -> Net-(F1-Pad2)
- J1 pad 2: Net-(J1-Pad2) -> GND
- J3 pad 1: Earth -> AREF
- J3 pad 2: Net-(J3-Pad2) -> softpot-1
- J4 pad 1: Earth -> AREF
- J4 pad 2: Net-(J4-Pad2) -> softpot-2
- R10 pad 1: 5V -> Net-(R10-Pad1)
- R10 pad 2: SDA -> 12V_FILT
- R11 pad 1: Net-(R11-Pad1) -> BARREL_DETECT
- R11 pad 2: 5V -> GND
- R21 pad 1: Net-(R8-Pad1) -> Net-(R21-Pad1)
- R21 pad 2: Earth -> GND
- R3 pad 1: 3.3V -> 5VA_MCU
- R5 pad 1: 5V -> Net-(D16-Pad2)
- R5 pad 2: Net-(J12-Pad4) -> Net-(D16-Pad1)
- R6 pad 1: Net-(J12-Pad5) -> Net-(D2-Pad2)
- R6 pad 2: Net-(R6-Pad2) -> Net-(J2-Pad3)
- R7 pad 1: Net-(J11-Pad4) -> Net-(D2-Pad1)
- R7 pad 2: Net-(D1-Pad1) -> Net-(J2-Pad2)
- R9 pad 1: 5V -> D-
- R9 pad 2: SCL -> Net-(D2-Pad1)
- U1 pad 1: Net-(J1-Pad2) -> Net-(C15-Pad2)
- U1 pad 2: Net-(J2-Pad2) -> Net-(C15-Pad1)
- U1 pad 3: Net-(J3-Pad2) -> Net-(C10-Pad1)
- U1 pad 4: Net-(J4-Pad2) -> Net-(Q3-Pad4)
- U1 pad 5: Net-(J5-Pad2) -> GND
- U1 pad 6: Net-(J6-Pad2) -> Net-(R12-Pad2)
- U1 pad 7: Net-(J7-Pad2) -> Net-(R10-Pad1)
- U1 pad 8: Net-(J8-Pad2) -> 12V_FILT
- U1 pad 9: 5V -> GND
- U2 pad 1: MIDI-OUT -> Net-(C16-Pad2)
- U2 pad 11: Earth -> MCU1-MCU3_GPIO
- U2 pad 13: Earth -> Net-(R18-Pad1)
- U2 pad 14: 5V -> Net-(TP4-Pad1)
- U2 pad 2: Net-(U2-Pad2) -> Net-(C17-Pad2)
- U2 pad 3: Net-(U2-Pad2) -> GND
- U2 pad 4: Net-(R6-Pad2) -> 5V_MCU
- U2 pad 5: Net-(R11-Pad1) -> BTN1b
- U2 pad 6: Net-(U2-Pad6) -> PROG_CTRL_2
- U2 pad 7: Earth -> PROG_CTRL_1
- U2 pad 8: MIDI-IN -> MCU1-MCU3_TX
- U2 pad 9: Net-(U2-Pad6) -> RST_2560
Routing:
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
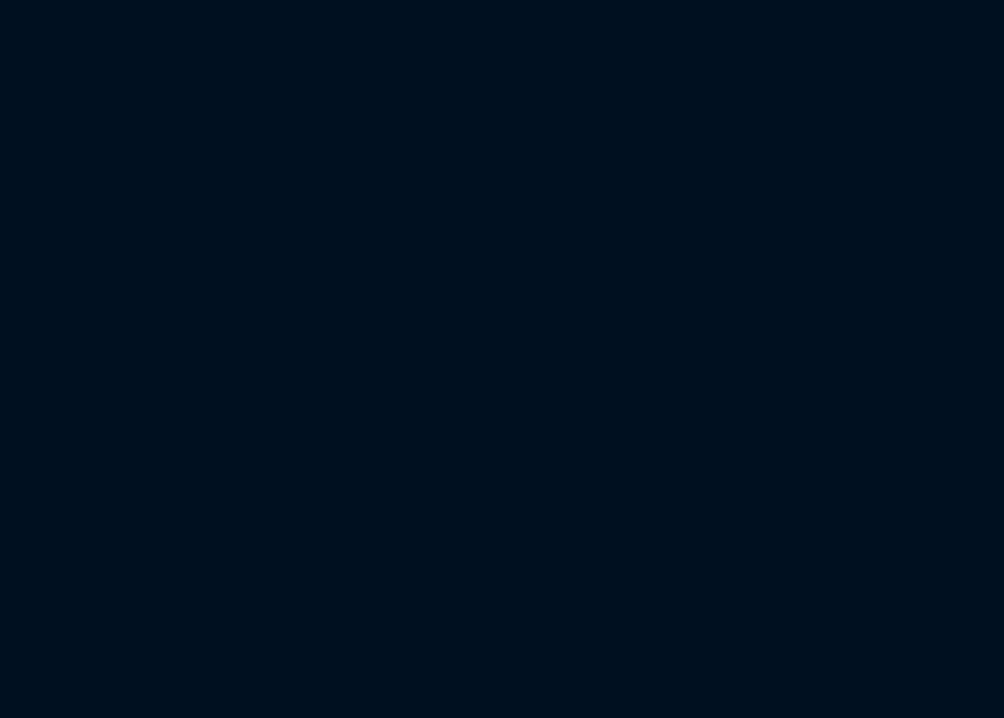
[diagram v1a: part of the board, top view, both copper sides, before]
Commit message: Minor schematic and library changes
Fixes some typos; changes oscillators to be common to all MCUs; SMD for MIDI opto input
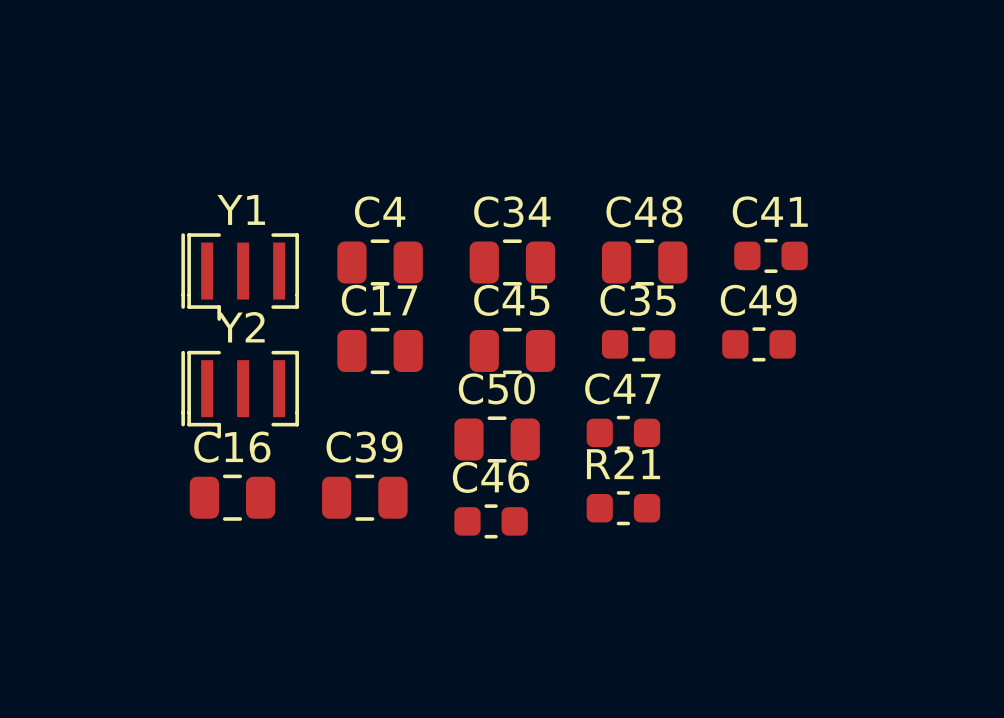
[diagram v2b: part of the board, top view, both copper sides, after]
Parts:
- added C16: DNP-1uF 25V, Capacitor_SMD:C_0805_2012Metric, F.Cu at (244.5, 68.4)
- added C17: 1uF 25V, Capacitor_SMD:C_0805_2012Metric, F.Cu at (249.4, 63.5)
- added C34: 1uF 25V, Capacitor_SMD:C_0805_2012Metric, F.Cu at (253.8, 60.5)
- added C35: 100nf, Capacitor_SMD:C_0603_1608Metric, F.Cu at (258.1, 63.3)
- added C39: 1uF 25V, Capacitor_SMD:C_0805_2012Metric, F.Cu at (248.9, 68.4)
- added C4: DNP-1uF 25V, Capacitor_SMD:C_0805_2012Metric, F.Cu at (249.4, 60.5)
- added C41: 100nf, Capacitor_SMD:C_0603_1608Metric, F.Cu at (262.5, 60.3)
- added C45: 1uF 25V, Capacitor_SMD:C_0805_2012Metric, F.Cu at (253.8, 63.5)
- added C46: 100nf, Capacitor_SMD:C_0603_1608Metric, F.Cu at (253.1, 69.2)
- added C47: 100nf, Capacitor_SMD:C_0603_1608Metric, F.Cu at (257.5, 66.2)
- added C48: 1uF 25V, Capacitor_SMD:C_0805_2012Metric, F.Cu at (258.3, 60.5)
- added C49: 100nf, Capacitor_SMD:C_0603_1608Metric, F.Cu at (262.1, 63.3)
- added C50: 1uF 25V, Capacitor_SMD:C_0805_2012Metric, F.Cu at (253.3, 66.4)
- added R21: 19.1k, Resistor_SMD:R_0603_1608Metric, F.Cu at (257.5, 68.7)
- added Y1: 16MHz, Crystal:Resonator_SMD_muRata_CSTxExxV-3Pin_3.0x1.1mm, F.Cu at (244.9, 60.8)
- added Y2: 16MHz, Crystal:Resonator_SMD_muRata_CSTxExxV-3Pin_3.0x1.1mm, F.Cu at (244.9, 64.7)
- Y3: value 16MHz CSTNE16M0V530000R0 -> 16MHz
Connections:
- net /SHIELD renamed Net-(C4-Pad1)
- C33 pad 1: MCU2_RST -> MCU3_RST
- D16 pad 3: Earth -> GND
- D2 pad 3: Earth -> GND
- D3 pad 3: Earth -> GND
- J6 pad 2: Net-(J6-Pad2) -> Net-(C16-Pad1)
- R28 pad 1: MCU2_RST -> 5V_MCU
- R28 pad 2: 5V_MCU -> MCU3_RST
- U2 pad 1: Net-(C16-Pad2) -> Net-(U2-Pad1) (x2)
- U2 pad 2: Net-(C17-Pad2) -> Net-(U2-Pad2) (x2)
- U5 pad 1: Net-(C34-Pad2) -> Net-(U5-Pad1)
- U5 pad 2: Net-(C35-Pad2) -> Net-(U5-Pad2)
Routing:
- net Net-(U2-Pad2): track 0.00 -> 2.96 mm
- net Net-(C17-Pad2): track 2.96 -> 0.00 mm
